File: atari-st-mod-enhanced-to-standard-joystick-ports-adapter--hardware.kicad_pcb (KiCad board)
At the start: 4 copper layers, 100 x 100 mm, 52 parts, among them J1 Joy0/Mouse, J2 Joy1, J3 OLED 128×64, J4 Enhanced Joystick Port, J5 Joy0/Mouse, J6 Joy1, Q1 1<Vgsth<2, Low Rdson, Vds >10, Q10 1<Vgsth<2, Low Rdson, Vds >10, Q2 1<Vgsth<2, Low Rdson, Vds >10, Q3 1<Vgsth<2, Low Rdson, Vds >10, Q4 1<Vgsth<2, Low Rdson, Vds >10, Q5 1<Vgsth<2, Low Rdson, Vds >10, Q6 1<Vgsth<2, Low Rdson, Vds >10, Q7 1<Vgsth<2, Low Rdson, Vds >10, Q8 1<Vgsth<2, Low Rdson, Vds >10, Q9 1<Vgsth<2, Low Rdson, Vds >10, SW1 Reset, SW2 Selector, SW3 Activate/Change, SW4 Cancel, U1 LM4040DBZ-3

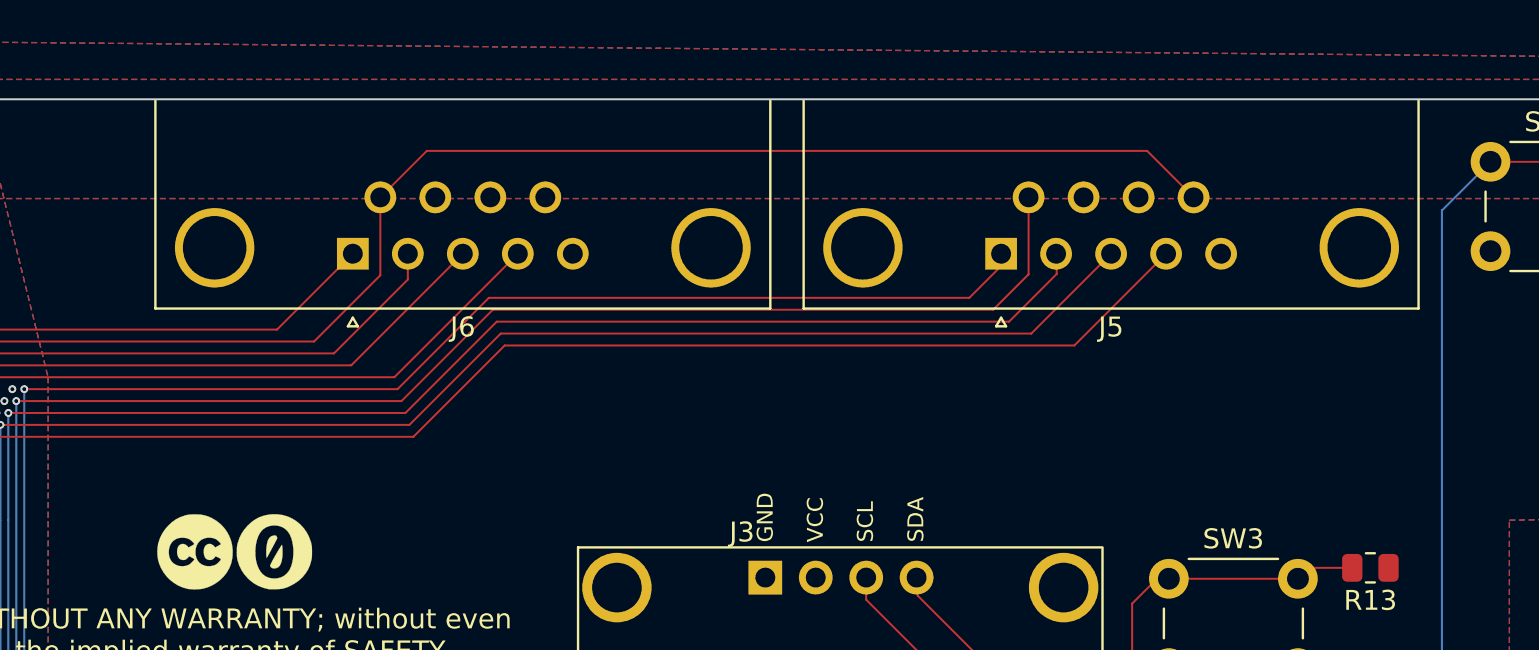
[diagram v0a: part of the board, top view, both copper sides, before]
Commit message: change footprint of J5/J6 for plastic db9 socket
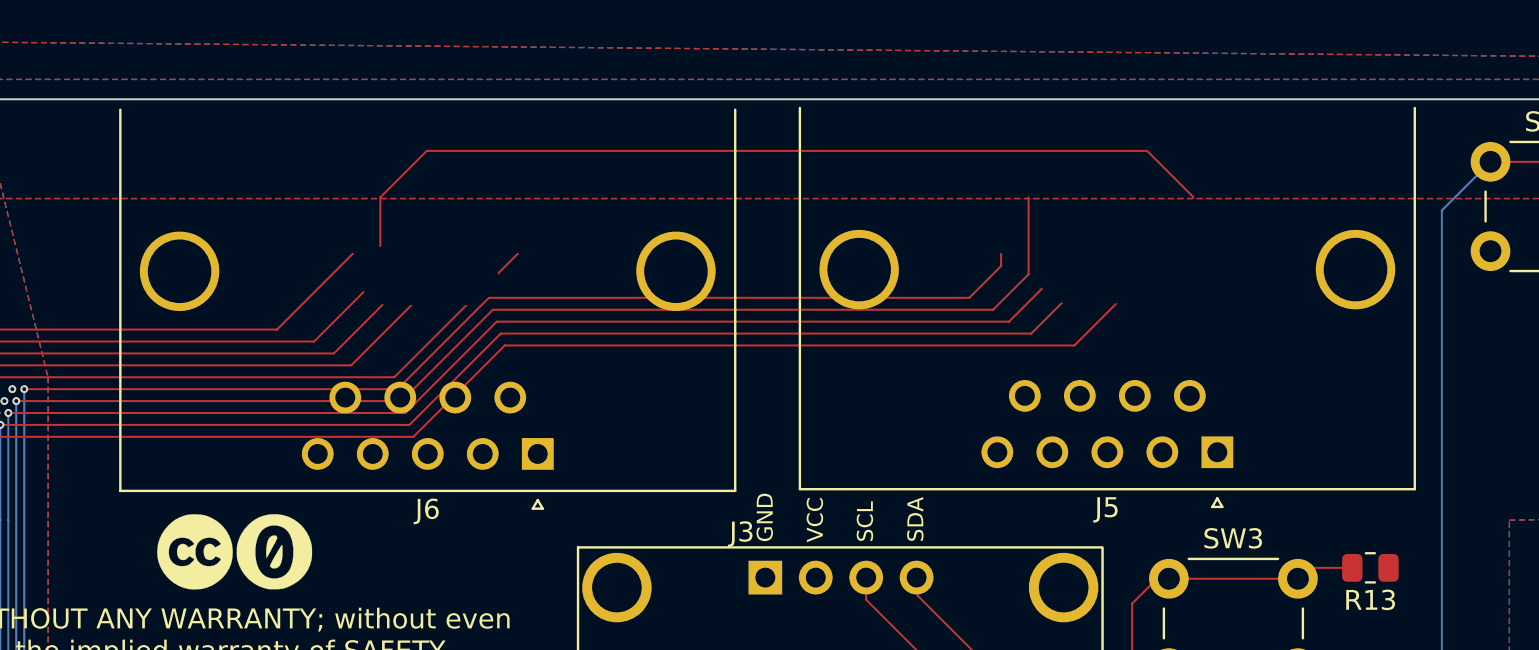
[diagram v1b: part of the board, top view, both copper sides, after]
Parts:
- J5, J6: footprint Connector_Dsub:DSUB-9_Female_Horizontal_P2.77x2.84mm_EdgePinOffset4.94mm_Housed_MountingHolesOffset7.48mm -> atari-interconnect:Joystick_Port_DSUB-9_Male_Horizontal_P2.77x2.84mm_EdgePinOffset14.56mm_Housed_MountingHolesOffset8.2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
- moved J5 14.8 mm to (117.7, 67.8)
- moved J6 13.7 mm to (83.5, 67.9)

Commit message: pcb session 2023-12-10T09:18:17+01:00 : working on legacy joystick port
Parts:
- moved J5 0.10 mm to (117.7, 67.9)
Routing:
- net /j0_right: track 193.4 -> 138.0 mm, vias 1 -> 0
- net /j0_left: track 191.5 -> 138.9 mm, vias 1 -> 0
- net /j0_fire: track 197.6 -> 145.8 mm, vias 1 -> 0
- net /j0_down: track 190.7 -> 140.3 mm, vias 1 -> 0
- net /j0_up: track 189.5 -> 142.3 mm, vias 1 -> 0
- net /j1_fire: track 207.2 -> 187.9 mm
- net /j1_right: track 131.7 -> 119.3 mm
- net /j1_left: track 132.5 -> 123.3 mm
- net /j1_down: track 131.8 -> 126.9 mm
- net GND2: vias 7 -> 0
- removed copper zone on In2.Cu, net GND2

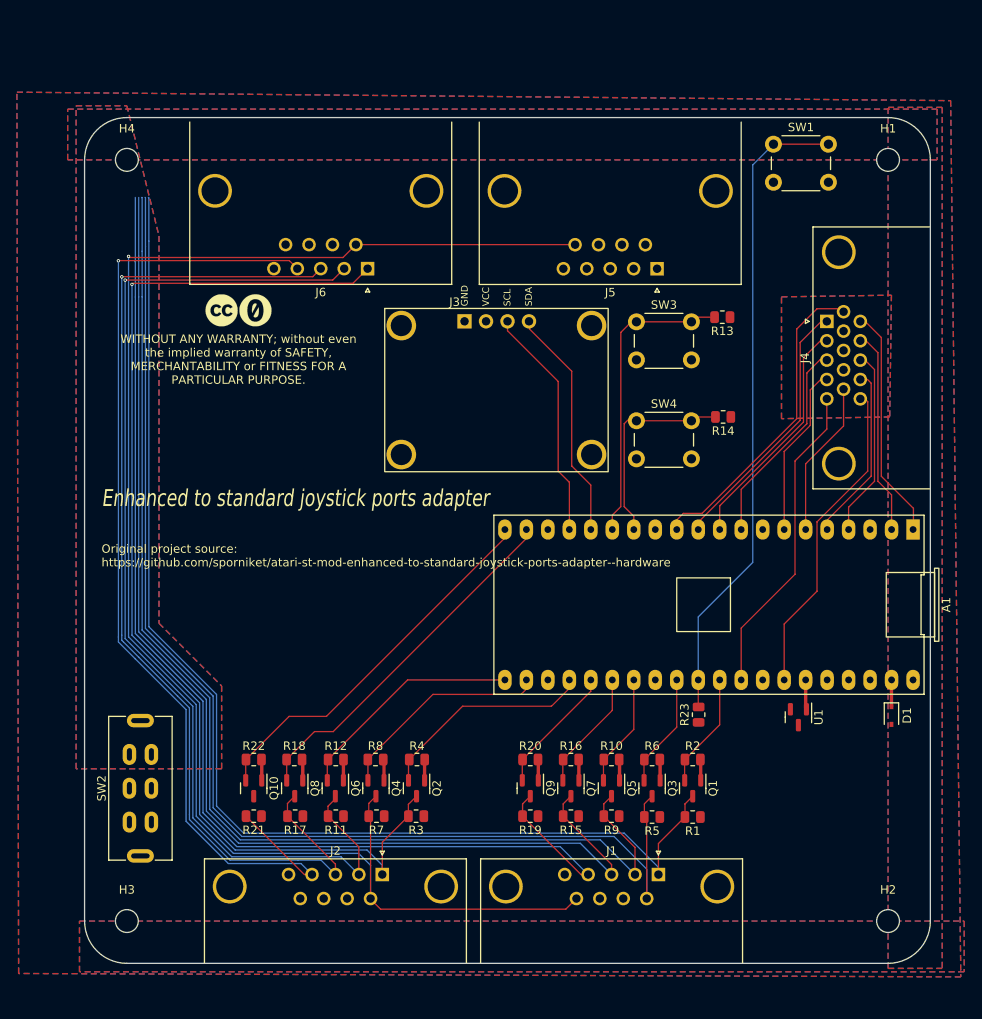
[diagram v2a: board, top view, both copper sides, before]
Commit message: cleaning the trace pathes
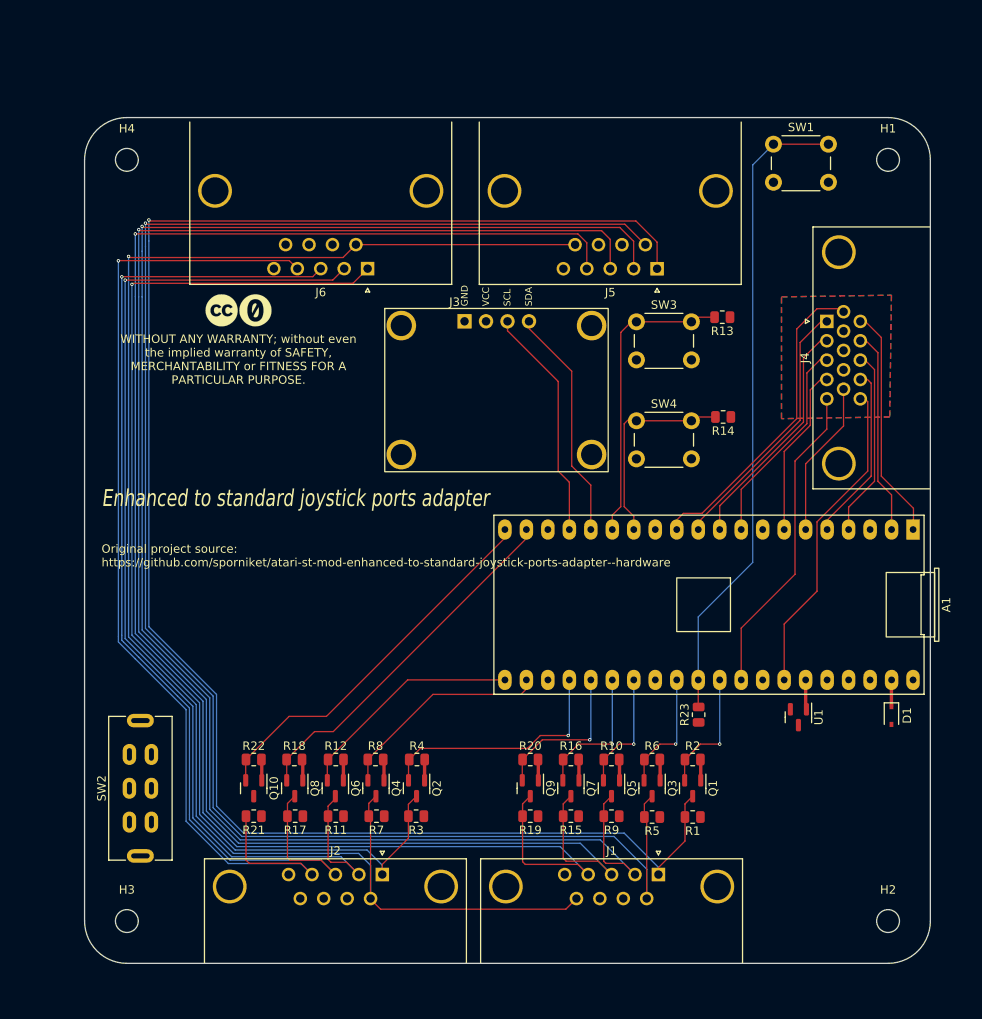
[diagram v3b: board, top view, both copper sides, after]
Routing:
- net /j0_up: track 142.3 -> 204.0 mm, vias 0 -> 1
- net /j0_down: track 140.3 -> 200.2 mm, vias 0 -> 1
- net /j0_left: track 138.9 -> 197.0 mm, vias 0 -> 1
- net /j0_fire: track 145.8 -> 202.9 mm, vias 0 -> 1
- net /j0_right: track 138.0 -> 193.7 mm, vias 0 -> 1
- net /right0: track 15.2 -> 18.5 mm, vias 0 -> 1
- net /up0: track 13.6 -> 16.8 mm, vias 0 -> 1
- net /up1: track 25.9 -> 29.1 mm, vias 0 -> 1
- net /j1_right: track 119.3 -> 122.3 mm
- net /left0: track 14.3 -> 16.6 mm, vias 0 -> 1
- net /j1_left: track 123.3 -> 125.5 mm
- net /fire0: track 13.5 -> 14.6 mm, vias 0 -> 1
- net /j1_down: track 126.9 -> 128.0 mm
- net /down0: track 13.4 -> 14.4 mm, vias 0 -> 1
- removed copper zone on In1.Cu, net GND
- removed copper zone on B.Cu, net GND1
- removed copper zone on F.Cu, net GND1
- removed copper zone on B.Cu, net GND2
- removed copper zone on F.Cu, net GND2
- removed copper zone on In1.Cu, net GND2

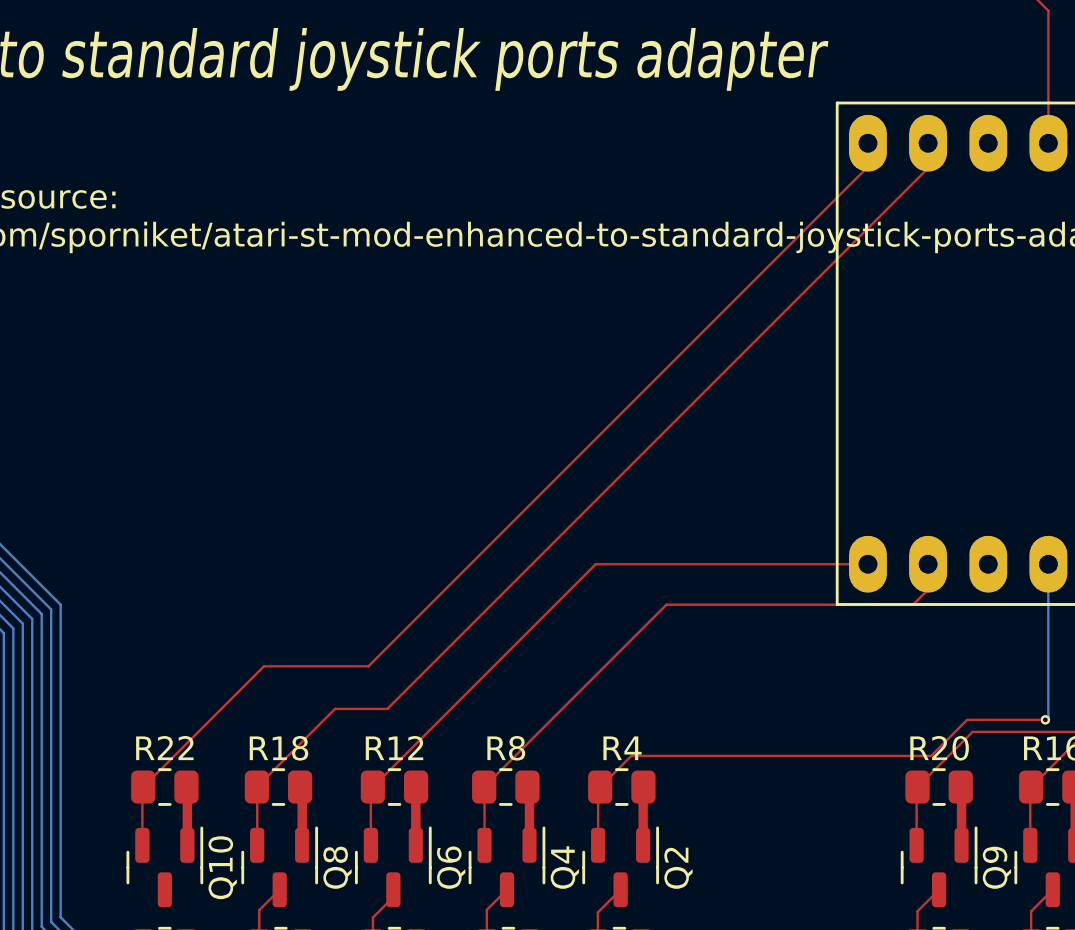
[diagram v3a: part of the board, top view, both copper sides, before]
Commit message: cleaning the trace pathes
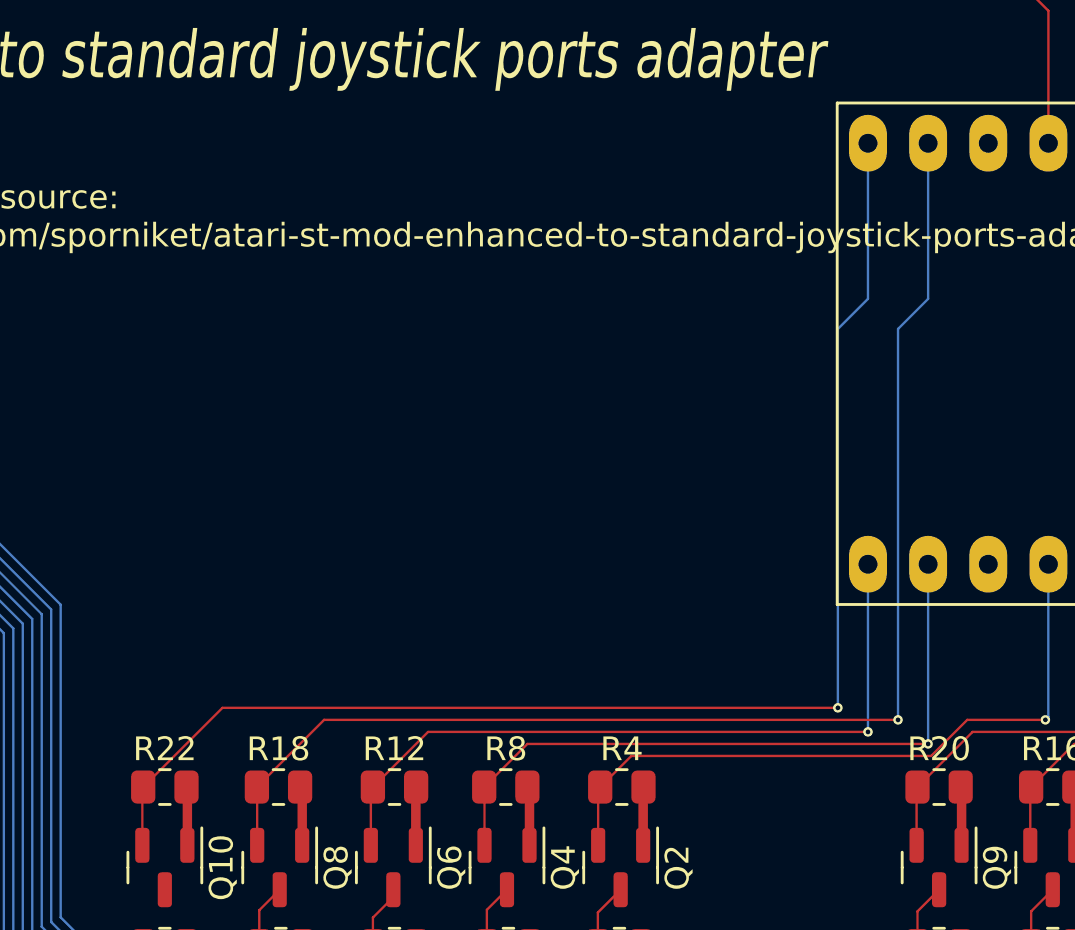
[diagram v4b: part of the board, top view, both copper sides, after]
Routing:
- net /left1: track 42.7 -> 55.6 mm, vias 0 -> 1
- net /right1: track 44.9 -> 57.6 mm, vias 0 -> 1
- net /down1: track 27.3 -> 31.5 mm, vias 0 -> 1
- net /fire1: track 25.7 -> 29.6 mm, vias 0 -> 1
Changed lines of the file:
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@@
   (segment (start 107.188 123.063) (end 107.19 123.063) (width 0.1) (layer "B.Cu") (net 7))
   (segment (start 107.19 123.063) (end 107.316 122.937) (width 0.1) (layer "B.Cu") (net 7))
-  (segment (start 99.696 116.49) (end 88.1975 116.49) (width 0.1) (layer "F.Cu") (net 8))
+  (segment (start 78.7875 125.9) (end 81.1165 123.571) (width 0.1) (layer "F.Cu") (net 8))
   (segment (start 78.7 128.3625) (end 78.7 125.9875) (width 0.1) (layer "F.Cu") (net 8))
   (segment (start 78.7 125.9875) (end 78.7875 125.9) (width 0.1) (layer "F.Cu") (net 8))
-  (segment (start 88.1975 116.49) (end 78.7875 125.9) (width 0.1) (layer "F.Cu") (net 8))
-  (segment (start 102.236 99.764) (end 79.4 122.6) (width 0.1) (layer "F.Cu") (net 9))
-  (segment (start 77.1875 122.6) (end 73.8875 125.9) (width 0.1) (layer "F.Cu") (net 9))
+  (segment (start 81.1165 123.571) (end 99.696 123.571) (width 0.1) (layer "F.Cu") (net 8))
+  (via (at 99.696 123.571) (size 0.4) (drill 0.2) (layers "F.Cu" "B.Cu") (net 8))
+  (segment (start 99.696 116.49) (end 99.696 123.571) (width 0.1) (layer "B.Cu") (net 8))
+  (segment (start 73.8875 125.9) (end 76.7245 123.063) (width 0.1) (layer "F.Cu") (net 9))
+  (segment (start 76.7245 123.063) (end 100.965 123.063) (width 0.1) (layer "F.Cu") (net 9))
   (segment (start 73.9 125.9125) (end 73.8875 125.9) (width 0.1) (layer "F.Cu") (net 9))
-  (segment (start 102.236 98.71) (end 102.236 99.764) (width 0.1) (layer "F.Cu") (net 9))
-  (segment (start 79.4 122.6) (end 77.1875 122.6) (width 0.1) (layer "F.Cu") (net 9))
   (segment (start 73.9 128.3625) (end 73.9 125.9125) (width 0.1) (layer "F.Cu") (net 9))
+  (via (at 100.965 123.063) (size 0.4) (drill 0.2) (layers "F.Cu" "B.Cu") (net 9))
+  (segment (start 102.236 105.282) (end 100.965 106.553) (width 0.1) (layer "B.Cu") (net 9))
+  (segment (start 100.965 106.553) (end 100.965 123.063) (width 0.1) (layer "B.Cu") (net 9))
+  (segment (start 102.236 98.71) (end 102.236 105.282) (width 0.1) (layer "B.Cu") (net 9))
   (segment (start 69.05 125.9375) (end 69.0875 125.9) (width 0.1) (layer "F.Cu") (net 10))
-  (segment (start 78.6 120.8) (end 74.1875 120.8) (width 0.1) (layer "F.Cu") (net 10))
-  (segment (start 74.1875 120.8) (end 69.0875 125.9) (width 0.1) (layer "F.Cu") (net 10))
+  (segment (start 69.0875 125.9) (end 72.4325 122.555) (width 0.1) (layer "F.Cu") (net 10))
   (segment (start 69.05 128.3625) (end 69.05 125.9375) (width 0.1) (layer "F.Cu") (net 10))
-  (segment (start 99.696 98.71) (end 99.696 99.704) (width 0.1) (layer "F.Cu") (net 10))
-  (segment (start 99.696 99.704) (end 78.6 120.8) (width 0.1) (layer "F.Cu") (net 10))
-  (segment (start 102.236 117.564) (end 101.6 118.2) (width 0.1) (layer "F.Cu") (net 11))
-  (segment (start 101.6 118.2) (end 91.1875 118.2) (width 0.1) (layer "F.Cu") (net 11))
+  (segment (start 72.4325 122.555) (end 98.425 122.555) (width 0.1) (layer "F.Cu") (net 10))
+  (via (at 98.425 122.555) (size 0.4) (drill 0.2) (layers "F.Cu" "B.Cu") (net 10))
+  (segment (start 99.696 98.71) (end 99.696 105.282) (width 0.1) (layer "B.Cu") (net 10))
+  (segment (start 99.696 105.282) (end 98.425 106.553) (width 0.1) (layer "B.Cu") (net 10))
+  (segment (start 98.425 106.553) (end 98.425 122.555) (width 0.1) (layer "B.Cu") (net 10))
+  (segment (start 85.3085 124.079) (end 102.236 124.079) (width 0.1) (layer "F.Cu") (net 11))
   (segment (start 83.5 125.9125) (end 83.4875 125.9) (width 0.1) (layer "F.Cu") (net 11))
   (segment (start 83.5 128.3625) (end 83.5 125.9125) (width 0.1) (layer "F.Cu") (net 11))
-  (segment (start 91.1875 118.2) (end 83.4875 125.9) (width 0.1) (layer "F.Cu") (net 11))
-  (segment (start 102.236 116.49) (end 102.236 117.564) (width 0.1) (layer "F.Cu") (net 11))
+  (segment (start 83.4875 125.9) (end 85.3085 124.079) (width 0.1) (layer "F.Cu") (net 11))
+  (via (at 102.236 124.079) (size 0.4) (drill 0.2) (layers "F.Cu" "B.Cu") (net 11))
+  (segment (start 102.236 116.49) (end 102.236 124.079) (width 0.1) (layer "B.Cu") (net 11))
   (segment (start 113.4 96) (end 112.396 97.004) (width 0.1) (layer "F.Cu") (net 12))
   (segment (start 115.25 74.15) (end 115.2 74.2) (width 0.1) (layer "F.Cu") (net 12))
